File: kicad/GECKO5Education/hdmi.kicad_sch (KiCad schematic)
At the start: 24 parts, among them J2 HDMI_A, J6 Conn_01x06_Socket, J7 Conn_01x02_Pin, U16 LTC2632CTS8-LZ12TRMPBF, U17 MAX11666AUBV, U3 SII164CTG64, U6 LFE5U-85F-6BG381x

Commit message: First version
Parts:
- removed C1, C2, C4, C5, C6: 100n, Capacitor_SMD:C_0402_1005Metric, symbol Device:C
- removed C3: 100n, Resistor_SMD:R_0402_1005Metric, symbol Device:C
- removed R4 (x6): 10k, Resistor_SMD:R_0402_1005Metric, symbol Device:R
- removed R4: 33k, Resistor_SMD:R_0402_1005Metric, symbol Device:R
- removed R4: 510E, Resistor_SMD:R_0402_1005Metric, symbol Device:R
- removed U3: SII164CTG64, gecko4education:QFP50P1200X1200X120-64N, symbol gecko5education:SII164CTG64
- added U3: SII9022ACNU, gecko4education:QFN72_10X10_LAT-M, symbol gecko5education:SII9022ACNU
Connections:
- net GND: now also U3.37 (SD3), U3.39 (SD2), U3.40 (SD1), U3.43 (CGND)
- net TX0+: now also U3.62 (TX0+)
- net TX0-: now also U3.61 (TX0-)
- net TX1+: now also U3.65 (TX1+)
- net TX1-: now also U3.64 (TX1-)
- net TX2+: now also U3.68 (TX2+)
- net TX2-: now also U3.67 (TX2-)
- net at J2.13 (CEC): now also U3.71 (CEC_A)
- net TXC+ renamed TCK+
- net TCK+: now also U3.59 (TXC+)
- net TXC- renamed TCK-
- net TCK-: now also U3.58 (TXC-)
- no-connect marks 7 -> 2

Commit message: small progress
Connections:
- net GND: now also U3.73 (GND)
- net at J2.19 (HPD): now also U3.54 (HPD)
- net CLK_49.152MHz: now reaches U3.38 (MCLK)
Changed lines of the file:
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@@
   (junction (at 106.68 88.9) (diameter 0) (color 0 0 0 0)
+  )
+  (junction (at 229.87 110.49) (diameter 0) (color 0 0 0 0)
   )
   (junction (at 266.7 95.25) (diameter 0) (color 0 0 0 0)
@@
     (stroke (width 0) (type default))
   )
+  (wire (pts (xy 251.46 82.55) (xy 228.6 82.55))
+    (stroke (width 0) (type default))
+  )
   (wire (pts (xy 229.87 120.65) (xy 229.87 125.73))
     (stroke (width 0) (type default))
@@
     (stroke (width 0) (type default))
   )
+  (wire (pts (xy 251.46 85.09) (xy 251.46 82.55))
+    (stroke (width 0) (type default))
+  )
   (wire (pts (xy 233.68 52.07) (xy 233.68 54.61))
     (stroke (width 0) (type default))
@@
     (stroke (width 0) (type default))
   )
+  (wire (pts (xy 228.6 34.29) (xy 229.87 34.29))
+    (stroke (width 0) (type default))
+  )
   (wire (pts (xy 106.68 88.9) (xy 110.49 88.9))
     (stroke (width 0) (type default))
@@
     (stroke (width 0) (type default))
   )
+  (wire (pts (xy 228.6 123.19) (xy 245.11 123.19))
+    (stroke (width 0) (type default))
+  )
   (wire (pts (xy 254 52.07) (xy 233.68 52.07))
     (stroke (width 0) (type default))
   )
+  (wire (pts (xy 254 85.09) (xy 251.46 85.09))
+    (stroke (width 0) (type default))
+  )
   (wire (pts (xy 114.3 44.45) (xy 116.84 44.45))
     (stroke (width 0) (type default))
@@
   )
   (wire (pts (xy 228.6 72.39) (xy 240.03 72.39))
+    (stroke (width 0) (type default))
+  )
+  (wire (pts (xy 229.87 34.29) (xy 229.87 110.49))
     (stroke (width 0) (type default))
   )
@@
     )
   )
+  (global_label "CLK_49.152MHz" (shape input) (at 245.11 123.19 0) (fields_autoplaced)
+    (effects (font (size 1.27 1.27)) (justify left))
+    (property "Intersheetrefs" "${INTERSHEET_REFS}" (at 263.0932 123.19 0)
+      (effects (font (size 1.27 1.27)) (justify left) hide)
+    )
+  )

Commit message: Added SII9022
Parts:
- added C1, C2, C3, C4, C5, C6: 100n, Resistor_SMD:R_0402_1005Metric, symbol Device:C
- added R4 (x3): 4k7, Resistor_SMD:R_0402_1005Metric, symbol Device:R
- added R4 (x2): 2k2, Resistor_SMD:R_0402_1005Metric, symbol Device:R
- added R4: 4k3, Resistor_SMD:R_0402_1005Metric, symbol Device:R
- added R4: 10k, Resistor_SMD:R_0402_1005Metric, symbol Device:R
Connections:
- net HDMI_Green5 is gone; now on net HDMI_Green3: U6.B20 (PT121B)
- net HDMI_Red4 is gone; now on net HDMI_Red3: U6.A17 (PT116A)
- net +3.3V: now also U3.21 (IOVCC), U3.3 (IOVCC), U3.46 (IOVCC), U3.69 (IO_SEL), U3.70 (VDDQ), C4.2, C5.2, C6.2, R4.2, R4.2
- net +5V: now also R4.1, R4.1
- net GND: now also U3.10 (D18), U3.11 (D17), U3.13 (D16), U3.19 (D10), U3.20 (D9), U3.23 (D8), U3.29 (D3), U3.30 (D2), U3.31 (D1), U3.32 (D0), U3.36 (SPDIF), U3.57 (IOGND), U3.63 (AGND), U3.9 (D19), C1.1, C2.1, C3.1, C4.1, C5.1, C6.1, R4.2, R4.2, R4.2
- net HDMI_Blue0: now also U3.28 (D4)
- net HDMI_Blue1: now also U3.27 (D5)
- net HDMI_Blue2: now also U3.25 (D6)
- net HDMI_Blue3: now also U3.24 (D7)
- net HDMI_Clk: now also U3.22 (IDCK)
- net HDMI_De: now also U3.33 (DE)
- net HDMI_Green0: now also U3.18 (D11)
- net HDMI_Green1: now also U3.17 (D12)
- net HDMI_Green2: now also U3.16 (D13)
- net HDMI_Green3: now also U3.15 (D14)
- net HDMI_Green4: now also U3.14 (D15), U6.B19 (PT119B)
- net HDMI_Hsync: now also U3.34 (HSYNC)
- net HDMI_Red0: now also U3.8 (D20), U6.A19 (PT121A); no longer U6.B19 (PT119B)
- net HDMI_Red1: now also U3.7 (D21), U6.A18 (PT119A); no longer U6.A19 (PT121A)
- net HDMI_Red2: now also U3.6 (D22)
- net HDMI_Red3: now also U3.4 (D23); no longer U6.A18 (PT119A)
- net HDMI_Vsync: now also U3.35 (VSYNC)
- net at J2.15 (SCL): now also U3.49 (DSCL), R4.2
- net at J2.16 (SDA): now also U3.48 (DSDA), R4.2
- net at J2.19 (HPD), U3.54 (HPD): now also R4.1
- net at U3.1 (CSCL): now also R4.1
- net +1V2: now reaches U3.12 (CVCC12)
- net +1V2: now also U3.26 (CVCC12), U3.42 (CVCC12), U3.47 (CVCC12), U3.5 (CVCC12), U3.53 (CVCC12), U3.60 (AVCC12), U3.66 (AVCC12), C1.2, C2.2, C3.2
- net at U3.2 (CSDA): now also R4.1
- net HDMI_Sdo: now reaches U3.41 (SD0)
- net HDMI_Ws: now reaches U3.44 (WS)
- net HDMI_Sck: now reaches U3.45 (SCK)
- net HDMI_nReset: now reaches U3.51 (RESET#)
- net at U3.56 (EXT_SWING): now also R4.1
- net at U3.72 (CI2CA): now also R4.1
- no-connect marks 2 -> 4

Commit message: updated
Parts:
- added C30: 100n, Resistor_SMD:R_0402_1005Metric, symbol Device:C
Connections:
- net +1V2: now also C30.2
- net GND: now also C30.1
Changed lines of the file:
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@@
   (junction (at 171.45 59.69) (diameter 0) (color 0 0 0 0)
   )
+  (junction (at 224.79 156.21) (diameter 0) (color 0 0 0 0)
+  )
   (junction (at 170.18 44.45) (diameter 0) (color 0 0 0 0)
   )
@@
   )
   (junction (at 231.14 21.59) (diameter 0) (color 0 0 0 0)
+  )
+  (junction (at 224.79 139.7) (diameter 0) (color 0 0 0 0)
   )
   (junction (at 229.87 125.73) (diameter 0) (color 0 0 0 0)
@@
     (stroke (width 0) (type default))
   )
+  (wire (pts (xy 231.14 139.7) (xy 224.79 139.7))
+    (stroke (width 0) (type default))
+  )
   (wire (pts (xy 232.41 102.87) (xy 232.41 44.45))
     (stroke (width 0) (type default))
@@
     (stroke (width 0) (type default))
   )
+  (wire (pts (xy 231.14 144.78) (xy 231.14 139.7))
+    (stroke (width 0) (type default))
+  )
   (wire (pts (xy 254 57.15) (xy 236.22 57.15))
     (stroke (width 0) (type default))
@@
     (stroke (width 0) (type default))
   )
+  (wire (pts (xy 231.14 152.4) (xy 231.14 156.21))
+    (stroke (width 0) (type default))
+  )
   (wire (pts (xy 171.45 113.03) (xy 171.45 123.19))
     (stroke (width 0) (type default))
@@
   )
   (wire (pts (xy 194.31 139.7) (xy 194.31 144.78))
+    (stroke (width 0) (type default))
+  )
+  (wire (pts (xy 231.14 156.21) (xy 224.79 156.21))
     (stroke (width 0) (type default))
   )
@@
         )
         (path "/47d58937-9286-45a8-b88f-d3fcc6f916c8/2168b384-5196-4073-b8ef-3119545e18e5"
+          (reference "C14") (unit 1)
+        )
+      )
+    )
+  )
+  (symbol (lib_id "Device:C") (at 231.14 148.59 180) (unit 1)
+    (in_bom yes) (on_board yes) (dnp no)
+    (property "Reference" "C30" (at 229.87 152.4 90)
+      (effects (font (size 1.27 1.27)))
+    )
+    (property "Value" "100n" (at 229.87 144.78 90)
+      (effects (font (size 1.27 1.27)))
+    )
+    (property "Footprint" "Resistor_SMD:R_0402_1005Metric" (at 230.1748 144.78 0)
+      (effects (font (size 1.27 1.27)) hide)
+    )
+    (property "Datasheet" "~" (at 231.14 148.59 0)
+      (effects (font (size 1.27 1.27)) hide)
+    )
+    (pin "1")
+    (pin "2")
+    (instances
+      (project "gecko5education"
+        (path "/47d58937-9286-45a8-b88f-d3fcc6f916c8/e24858e6-e459-4033-a46a-6eb11205cf28"
+          (reference "C30") (unit 1)
+        )
+        (path "/47d58937-9286-45a8-b88f-d3fcc6f916c8/2168b384-5196-4073-b8ef-3119545e18e5"

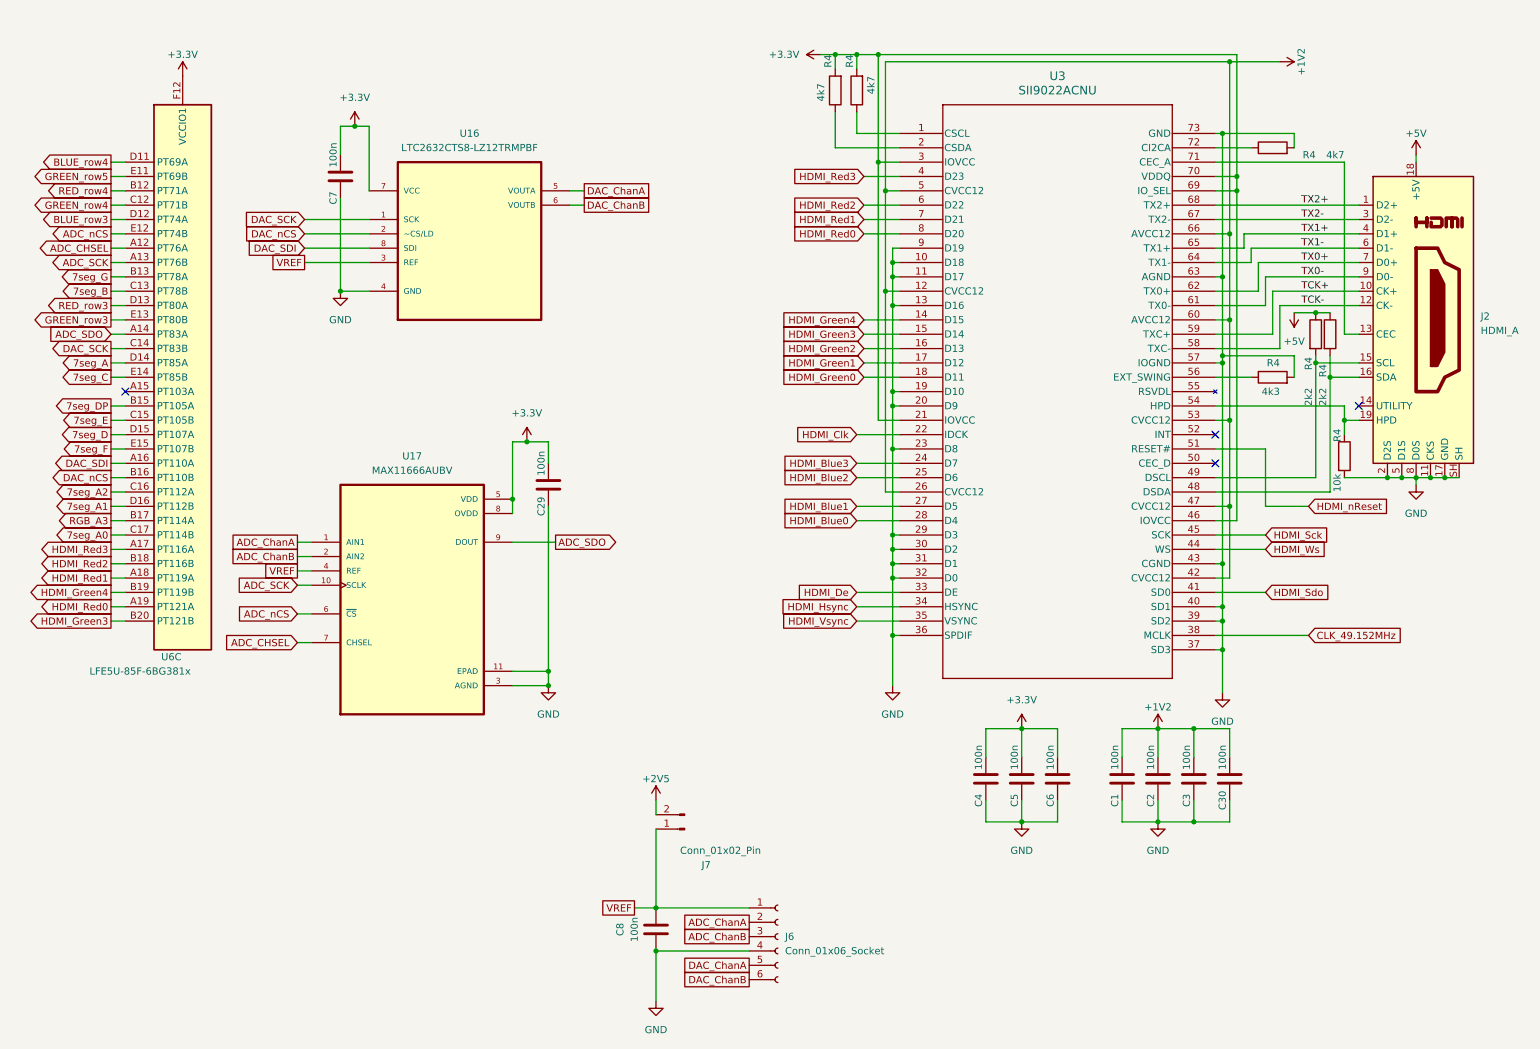
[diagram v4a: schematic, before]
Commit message: Added 2 add-on boards and updated GECKO5 to support olimex camera-OV7670 and an RTC.
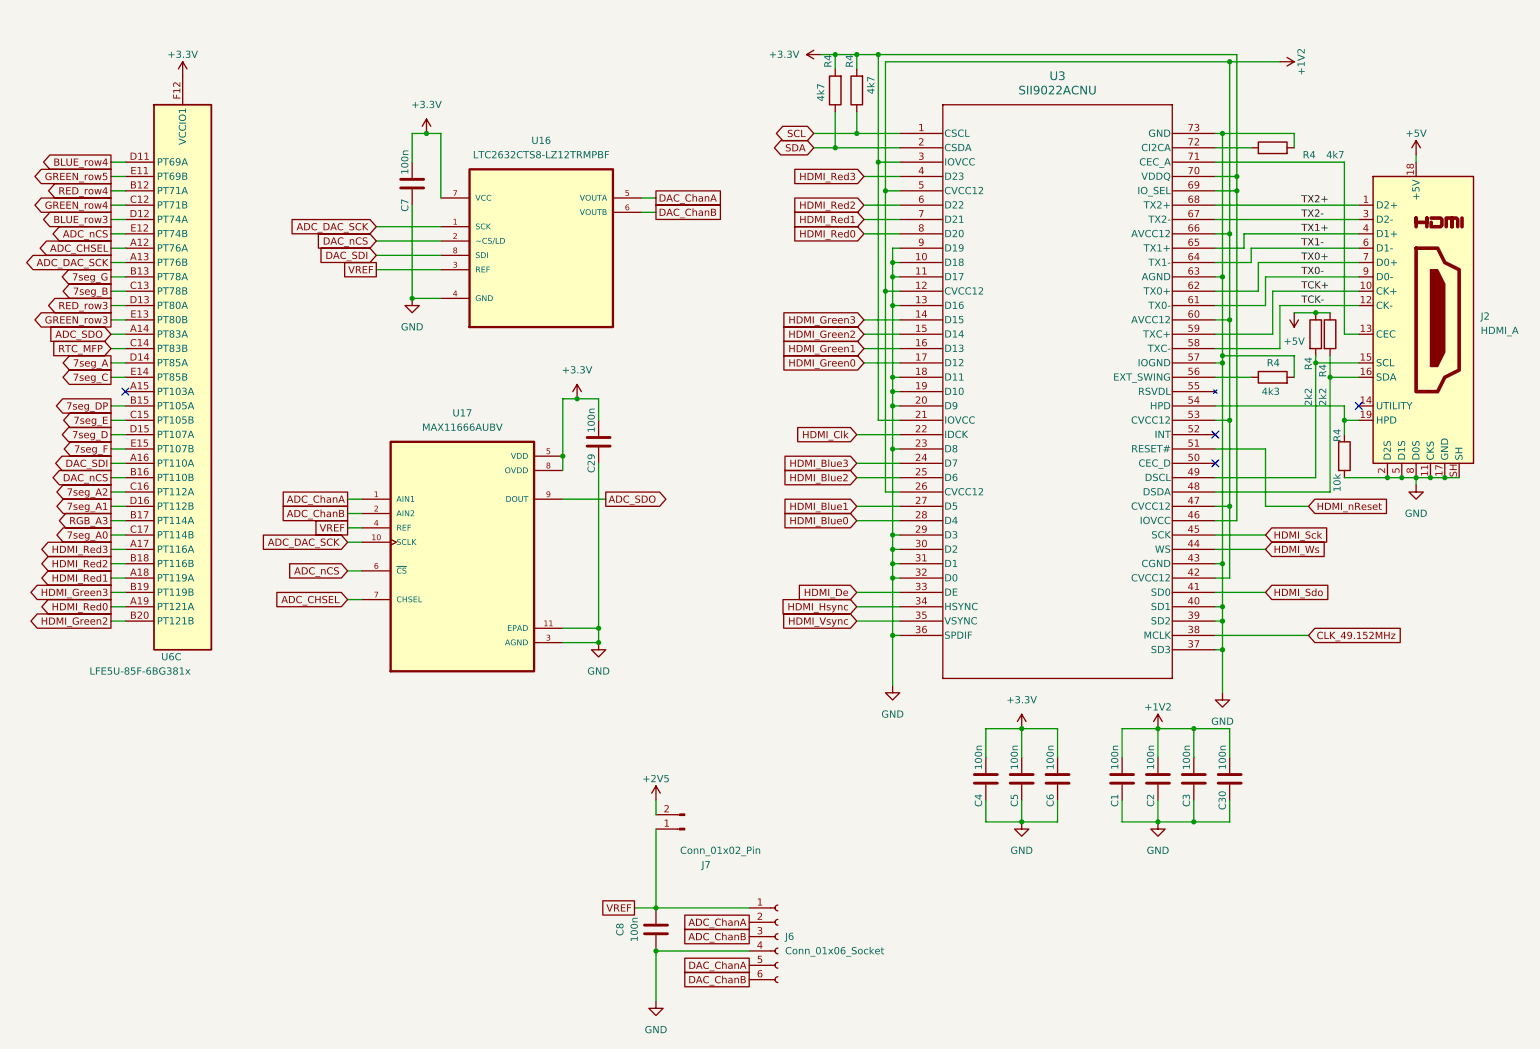
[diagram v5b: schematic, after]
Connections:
- net HDMI_Green4 is gone; now on net HDMI_Green3: U3.14 (D15), U6.B19 (PT119B)
- net GND: now also U3.18 (D11)
- net HDMI_Green0: now also U3.17 (D12); no longer U3.18 (D11)
- net HDMI_Green1: now also U3.16 (D13); no longer U3.17 (D12)
- net HDMI_Green2: now also U3.15 (D14), U6.B20 (PT121B); no longer U3.16 (D13)
- net HDMI_Green3: no longer U3.15 (D14), U6.B20 (PT121B)
- net SCL: now reaches R4.1, U3.1 (CSCL)
- net SDA: now reaches R4.1, U3.2 (CSDA)
- net ADC_SCK renamed ADC_DAC_SCK
- net ADC_DAC_SCK: now also U16.1 (SCK)
- net DAC_SCK renamed RTC_MFP
- net RTC_MFP: no longer U16.1 (SCK)
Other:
- moved on the sheet: C29, C7, U16, U17

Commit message: lates version
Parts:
- U17: value MAX11666AUBV -> MAX11102AUB+T
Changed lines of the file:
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@@
       (effects (font (size 1.27 1.27)))
     )
-    (property "Value" "MAX11666AUBV" (at 95.25 86.36 0)
+    (property "Value" "MAX11102AUB+T" (at 95.25 86.36 0)
       (effects (font (size 1.27 1.27)))
     )
